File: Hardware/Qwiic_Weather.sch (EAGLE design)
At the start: 21 parts, among them J1 Qwiic Right Angle, J3 Qwiic Right Angle, J4 PTH, U3 BME280

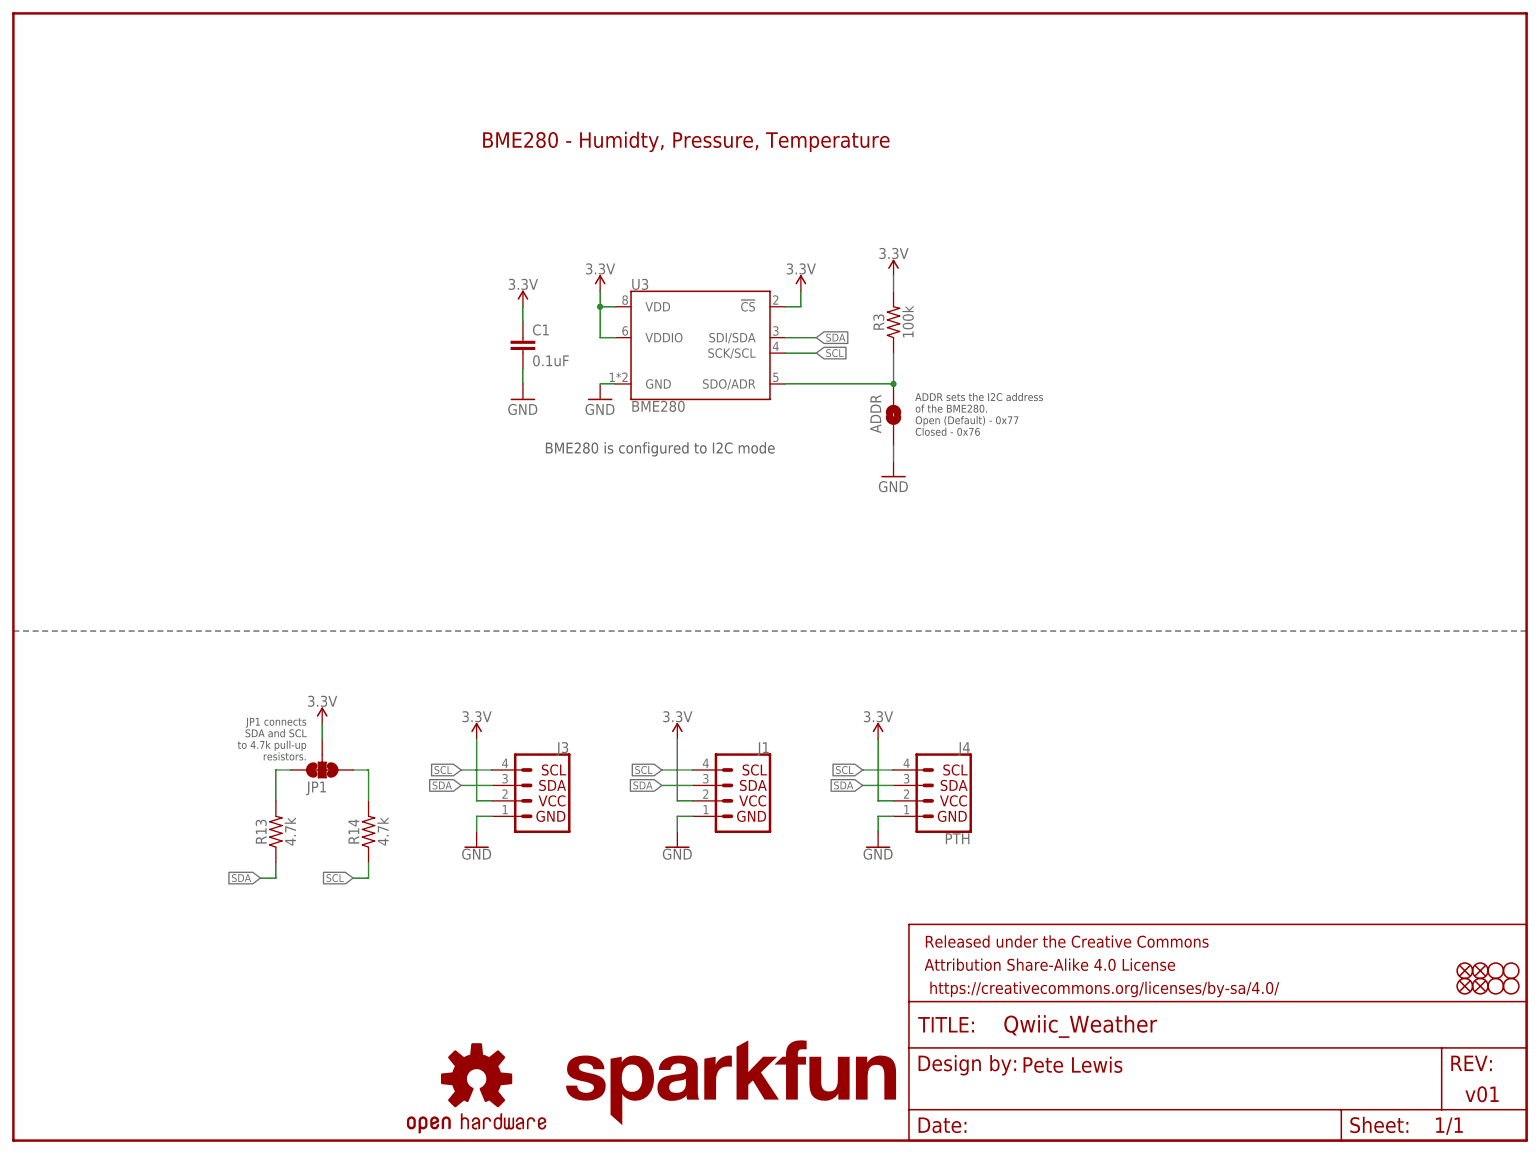
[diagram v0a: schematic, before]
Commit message: added SPI cabability and some prelim buzzard label work
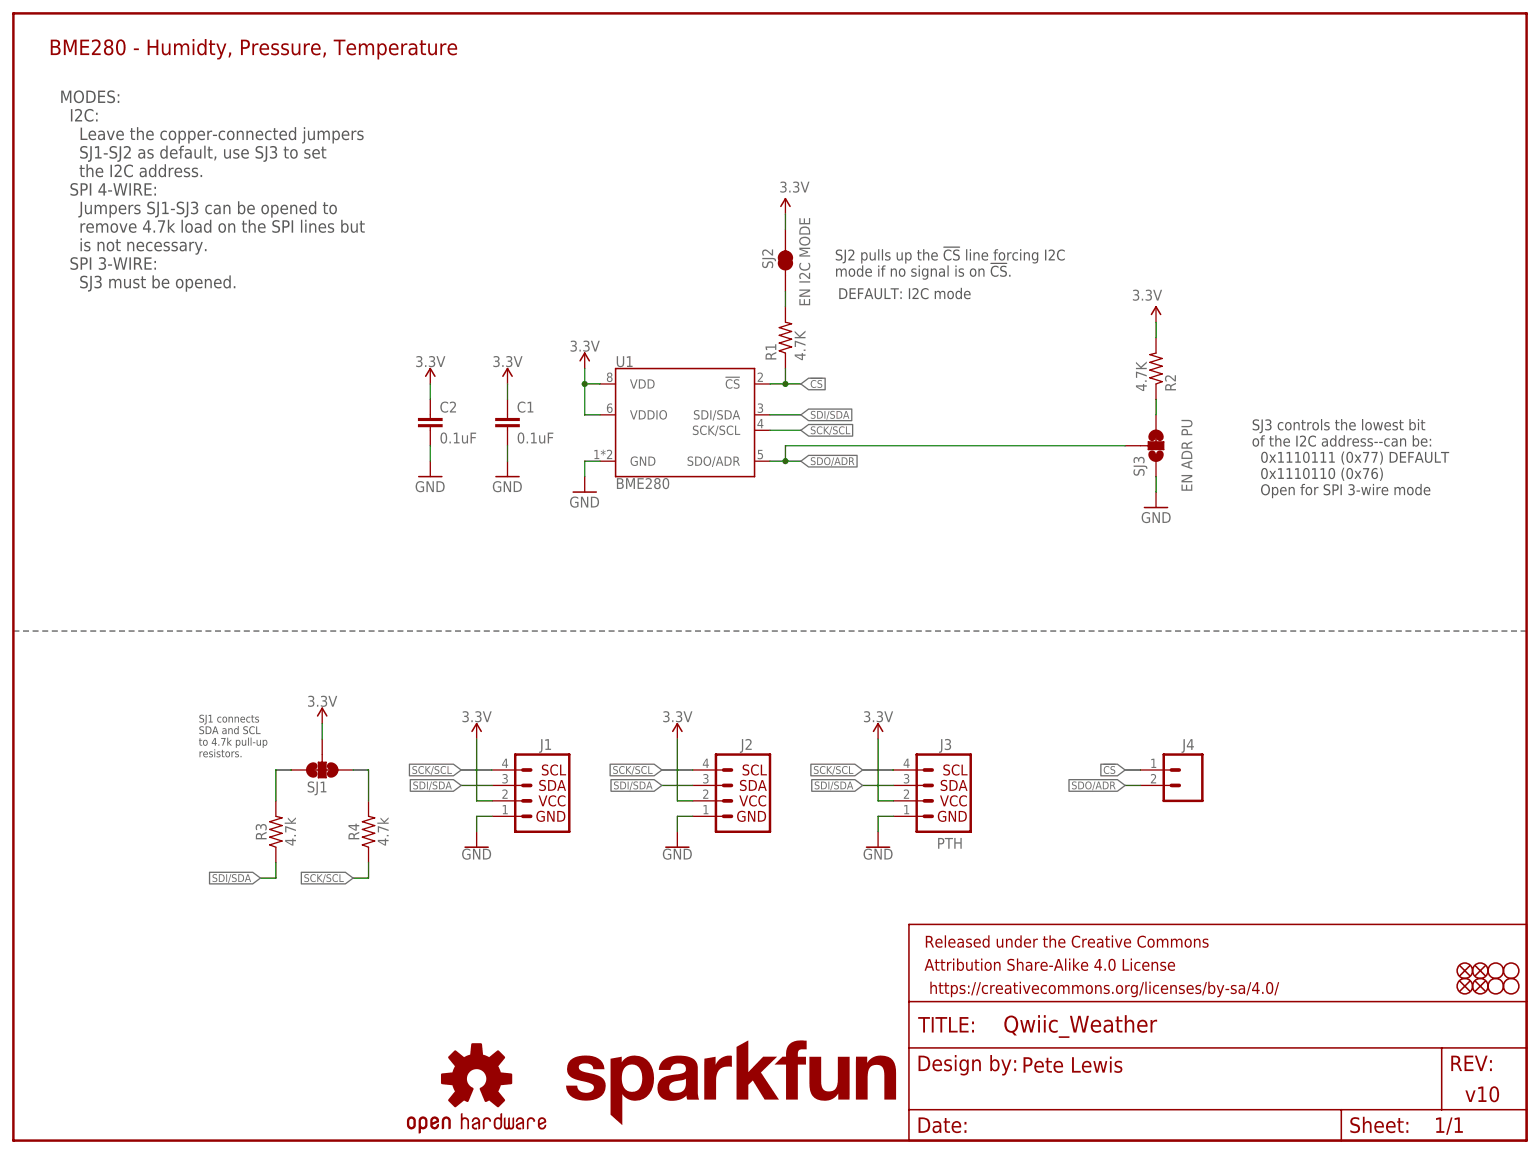
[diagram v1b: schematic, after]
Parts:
- removed ADDR: ADDR, SparkFun-Jumpers:JUMPER-SMT_2_NO_SILK
- removed R13: 4.7k, SparkFun-Resistors:4.7KOHM-0603-1/10W-1%
- removed U3: BME280, SparkFun-Sensors:BME280
- added C2: 0.1uF, SparkFun-Capacitors:0.1UF-0603-25V-(+80/-20%)
- added J2: QWIIC, SparkFun-Connectors:I2C_STANDARDQWIIC
- added R1, R2: 4.7K, SparkFun-Resistors:4.7KOHM-1/10W-1%(0603)
- added SJ2: EN I2C MODE, SparkFun-Passives:JUMPER-PAD-2-NC_BY_TRACE
- added SJ3: EN ADR PU, SparkFun-Passives:JUMPER-PAD-3-2OF3_NC_BY_TRACE_SMALL
- added U1: BME280, SparkFun-Sensors:BME280
- J1: value Qwiic Right Angle -> QWIIC
- J3: value Qwiic Right Angle -> PTH; device SparkFun-Connectors:I2C_STANDARDQWIIC -> SparkX:I2C_STANDARD_NO_SILK
- J4: value PTH -> (none); device SparkX:I2C_STANDARD_NO_SILK -> SparkFun-Connectors:CONN_021X02_NO_SILK
- R3: value 100k -> 4.7k; device SparkFun-Resistors:100KOHM-0603-1/10W-1% -> SparkFun-Resistors:4.7KOHM-0603-1/10W-1%
- renumbered JP1 to SJ1, R14 to R4
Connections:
- removed net SCL: J1.4, J3.4, J4.SCL, R4.1, U3.SCK/SCL
- removed net SDA: J1.3, J3.3, J4.SDA, R13.1, U3.SDI/SDA
- new net !CS: J4.1, R1.1, U1.!CS
- new net N$2: R2.1, SJ3.3
- new net N$6: R1.2, SJ2.1
- new net SCK/SCL: J1.4, J2.4, J3.SCL, R4.1, U1.SCK/SCL
- new net SDI/SDA: J1.3, J2.3, J3.SDA, R3.1, U1.SDI/SDA
- net 3.3V: now also C2.1, J2.2, J3.VCC, R2.2, SJ2.2, U1.VDD, U1.VDDIO; no longer J3.2, J4.VCC, R3.2, U3.!CS, U3.VDD, U3.VDDIO
- net GND: now also C2.2, J2.1, J3.GND, SJ3.1, U1.GND; no longer ADDR.1, J3.1, J4.GND, U3.GND
- net N$4: now also R3.2; no longer R13.2
- net SDO/ADR: now also J4.2, SJ3.2, U1.SDO/ADR; no longer ADDR.2, R3.1, U3.SDO/ADR
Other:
- note added: "DEFAULT: I2C mode"
- note added: "MODES: I2C: Leave the copper-connected jumpers SJ1-SJ2 as default, use SJ3 to set the I2C address. SPI 4-WIRE: Jumpers SJ1-SJ3 can be opened to remove 4.7k load on the SPI lines but is not necessary. SPI 3-WIRE: SJ3 must be opened."
- note added: "SJ1 connects SDA and SCL to 4.7k pull-up resistors."
- note added: "SJ2 pulls up the !CS! line forcing I2C mode if no signal is on !CS!."
- note added: "SJ3 controls the lowest bit of the I2C address--can be: 0x1110111 (0x77) DEFAULT 0x1110110 (0x76) Open for SPI 3-wire mode"
- note added: "v10"
- note removed: "ADDR sets the I2C address of the BME280. Open (Default) - 0x77 Closed - 0x76"
- note removed: "BME280 is configured to I2C mode"
- note removed: "JP1 connects SDA and SCL to 4.7k pull-up resistors."
- note removed: "v01"
- moved on the sheet: C1, J1, J3, R3

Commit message: Started routing board
About 50% done. Added a power LED, adjusted silk.
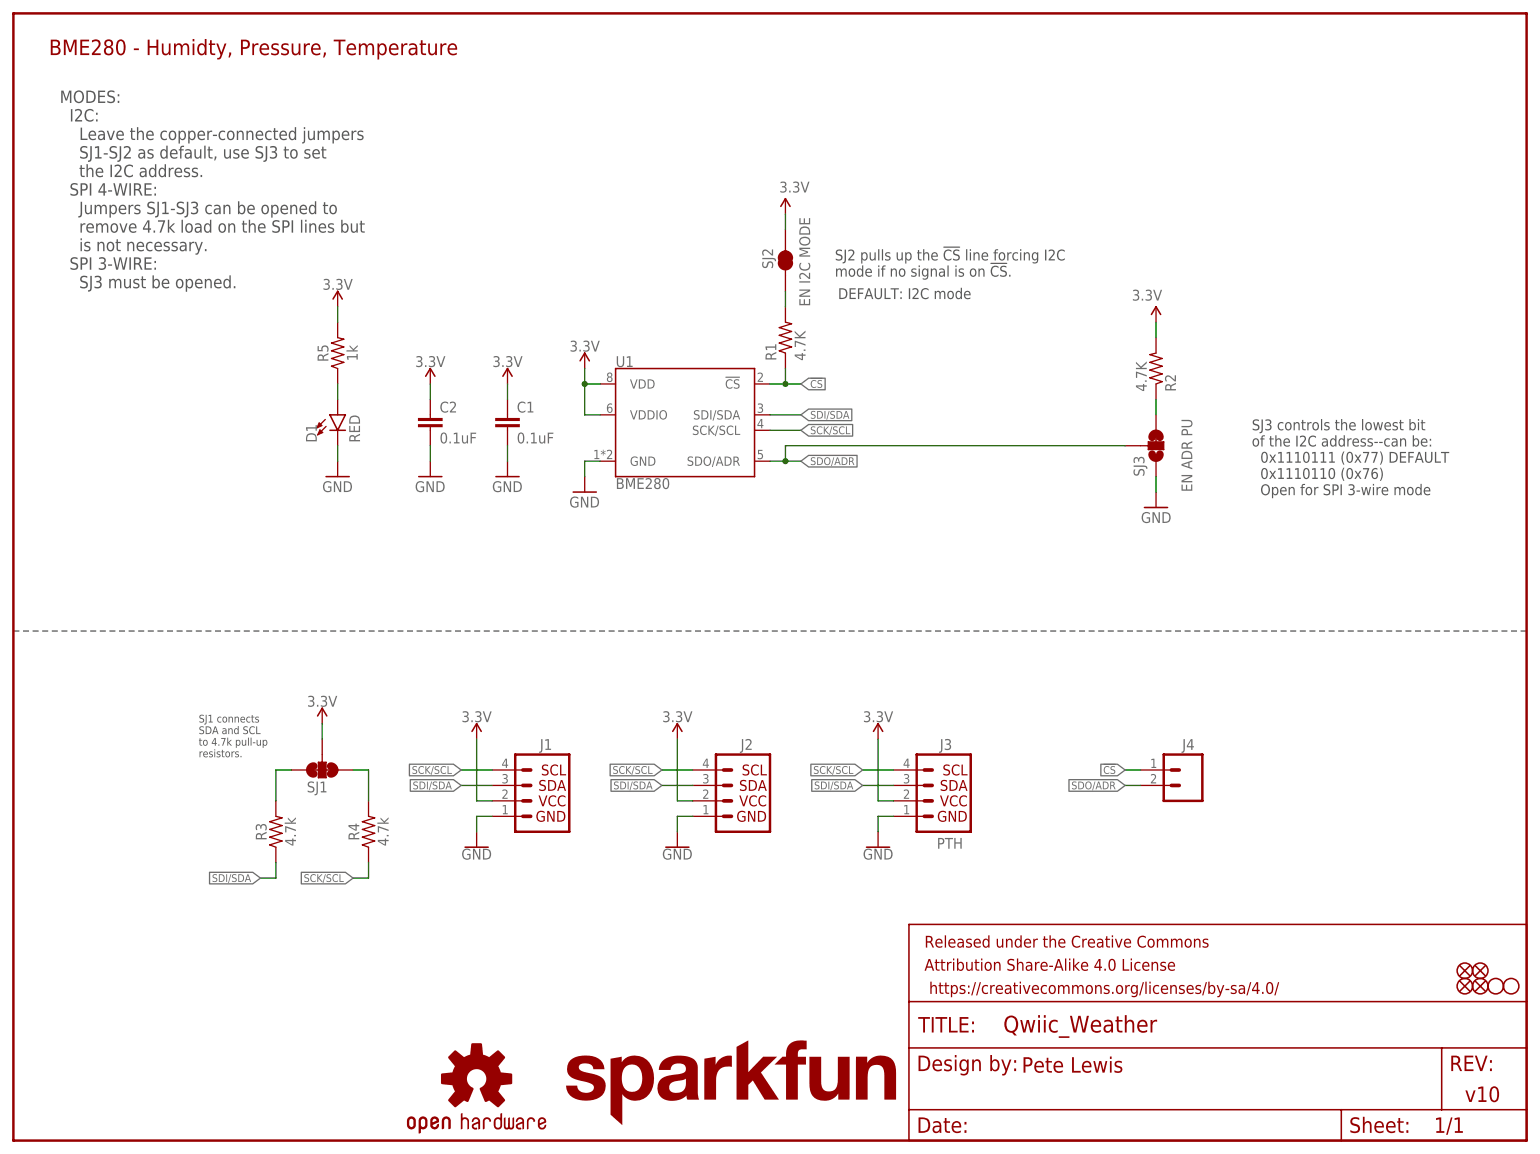
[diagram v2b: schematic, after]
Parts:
- removed H1, H3: STAND-OFF, SparkFun-Hardware:STAND-OFF
- added D1: RED, SparkFun-LED:LED-RED0603
- added R5: 1k, SparkFun-Resistors:1KOHM-0603-1/10W-1%
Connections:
- new net N$3: D1.A, R5.1
- net 3.3V: now also R5.2
- net GND: now also D1.C
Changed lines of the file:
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@@
 <?xml version="1.0" encoding="utf-8"?>
 <!DOCTYPE eagle SYSTEM "eagle.dtd">
-<eagle version="9.4.0">
+<eagle version="9.4.2">
 <drawing>
 <settings>
@@
 <part name="FD3" library="SparkFun-Aesthetics" deviceset="FIDUCIAL" device="1X2"/>
 <part name="FD4" library="SparkFun-Aesthetics" deviceset="FIDUCIAL" device="1X2"/>
-<part name="H1" library="SparkFun-Hardware" deviceset="STAND-OFF" device=""/>
-<part name="H3" library="SparkFun-Hardware" deviceset="STAND-OFF" device=""/>
 <part name="GND8" library="SparkFun-Aesthetics" deviceset="GND" device=""/>
 <part name="GND9" library="SparkFun-Aesthetics" deviceset="GND" device=""/>
@@
 <part name="SUPPLY5" library="SparkFun-Aesthetics" deviceset="3.3V" device=""/>
 <part name="GND5" library="SparkFun-Aesthetics" deviceset="GND" device=""/>
+<part name="D1" library="SparkFun-LED" deviceset="LED-RED" device="0603" value="RED"/>
+<part name="SUPPLY6" library="SparkFun-PowerSymbols" deviceset="3.3V" device=""/>
+<part name="GND3" library="SparkFun-Aesthetics" deviceset="GND" device=""/>
+<part name="R5" library="SparkFun-Resistors" deviceset="1KOHM" device="-0603-1/10W-1%" value="1k"/>
 </parts>
 <sheets>
@@
 <instance part="FD3" gate="G$1" x="241.3" y="27.94" smashed="yes"/>
 <instance part="FD4" gate="G$1" x="241.3" y="25.4" smashed="yes"/>
-<instance part="H1" gate="G$1" x="243.84" y="27.94" smashed="yes"/>
-<instance part="H3" gate="G$1" x="246.38" y="27.94" smashed="yes"/>
 <instance part="GND8" gate="1" x="93.98" y="106.68" smashed="yes">
 <attribute name="VALUE" x="91.44" y="104.14" size="1.778" layer="96"/>
@@
 <instance part="GND5" gate="1" x="187.96" y="104.14" smashed="yes" rot="MR0">
 <attribute name="VALUE" x="190.5" y="101.6" size="1.778" layer="96" rot="MR0"/>
+</instance>
+<instance part="D1" gate="G$1" x="53.34" y="119.38" smashed="yes">
+<attribute name="NAME" x="49.911" y="114.808" size="1.778" layer="95" font="vector" rot="R90"/>
+<attribute name="VALUE" x="55.245" y="114.808" size="1.778" layer="96" font="vector" rot="R90" align="top-left"/>
+</instance>
+<instance part="SUPPLY6" gate="G$1" x="53.34" y="137.16" smashed="yes">
+<attribute name="VALUE" x="53.34" y="139.954" size="1.778" layer="96" align="bottom-center"/>
+</instance>
+<instance part="GND3" gate="1" x="53.34" y="109.22" smashed="yes">
+<attribute name="VALUE" x="50.8" y="106.68" size="1.778" layer="96"/>
+</instance>
+<instance part="R5" gate="G$1" x="53.34" y="129.54" smashed="yes" rot="R90">
+<attribute name="NAME" x="51.816" y="129.54" size="1.778" layer="95" font="vector" rot="R90" align="bottom-center"/>
+<attribute name="VALUE" x="54.864" y="129.54" size="1.778" layer="96" font="vector" rot="R90" align="top-center"/>
 </instance>
 </instances>
@@
 <pinref part="SJ3" gate="G$1" pin="1"/>
 <wire x1="187.96" y1="106.68" x2="187.96" y2="109.22" width="0.1524" layer="91"/>
+</segment>
+<segment>
+<pinref part="D1" gate="G$1" pin="C"/>
+<pinref part="GND3" gate="1" pin="GND"/>
+<wire x1="53.34" y1="114.3" x2="53.34" y2="111.76" width="0.1524" layer="91"/>
 </segment>
 </net>
@@
 <wire x1="187.96" y1="132.08" x2="187.96" y2="134.62" width="0.1524" layer="91"/>
 </segment>
+<segment>
+<pinref part="SUPPLY6" gate="G$1" pin="3.3V"/>
+<pinref part="R5" gate="G$1" pin="2"/>
+<wire x1="53.34" y1="137.16" x2="53.34" y2="134.62" width="0.1524" layer="91"/>
+</segment>
 </net>
 <net name="N$4" class="0">
@@
 </segment>
 </net>
+<net name="N$3" class="0">
+<segment>
+<pinref part="R5" gate="G$1" pin="1"/>
+<pinref part="D1" gate="G$1" pin="A"/>
+<wire x1="53.34" y1="124.46" x2="53.34" y2="121.92" width="0.1524" layer="91"/>
+</segment>
+</net>
